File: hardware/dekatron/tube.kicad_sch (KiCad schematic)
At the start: 30 parts, among them J201 TUBE_ANODE, J202 TUBE, Q201 MMBTA42, Q202 MMBTA42, Q203 MMBTA92

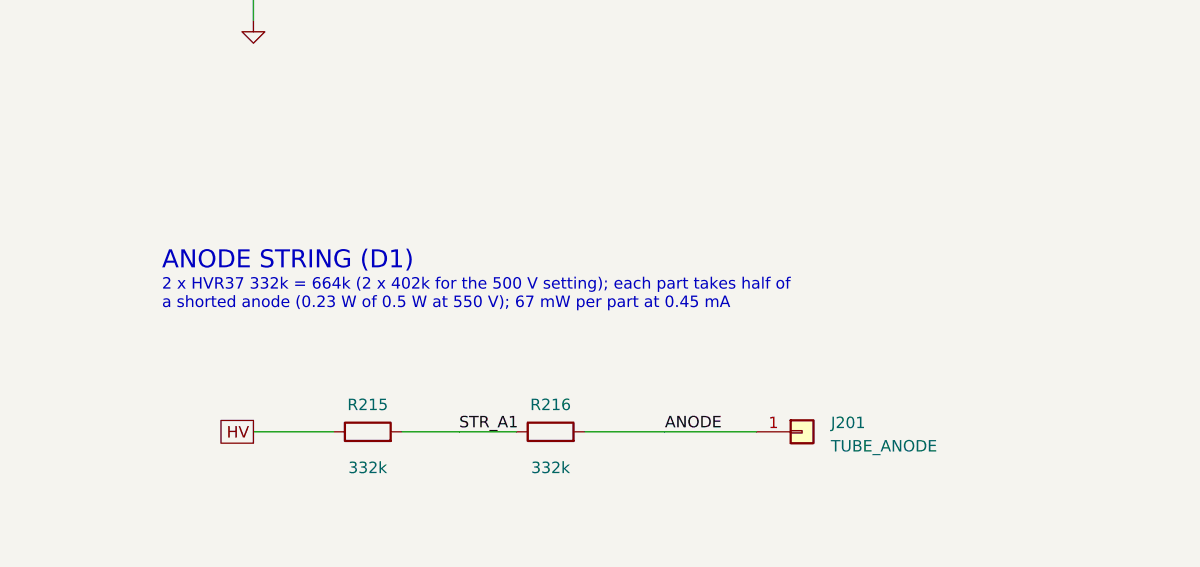
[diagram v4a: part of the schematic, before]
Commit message: Replace Vishay HVR25/HVR37 with Yageo HHV-25/HHV-50 (Mouser stock)
Same ratings (1600 V / 3500 V DC, 1 %, 200 ppm/K, 100k-68M E24/E96) and bodies
no larger (6.3 x 2.4 mm, 9.0 x 3.3 mm), so the 0207/0411 footprints stay.
Generator emits Yageo ordering codes (HHV-25FT-52-4M75 etc.); PCB fields
synced in place, ERC/DRC parity unchanged. hardware.md records the voltage
each leg actually needs at the 1.5x rule: >= 830 V for the two HV divider
tops, >= 415 V / 0.5 W for the anode pair, >= 303 V for the V_b-side parts.

Co-Authored-By: Claude Opus 5.5 <noreply@anthropic.com>
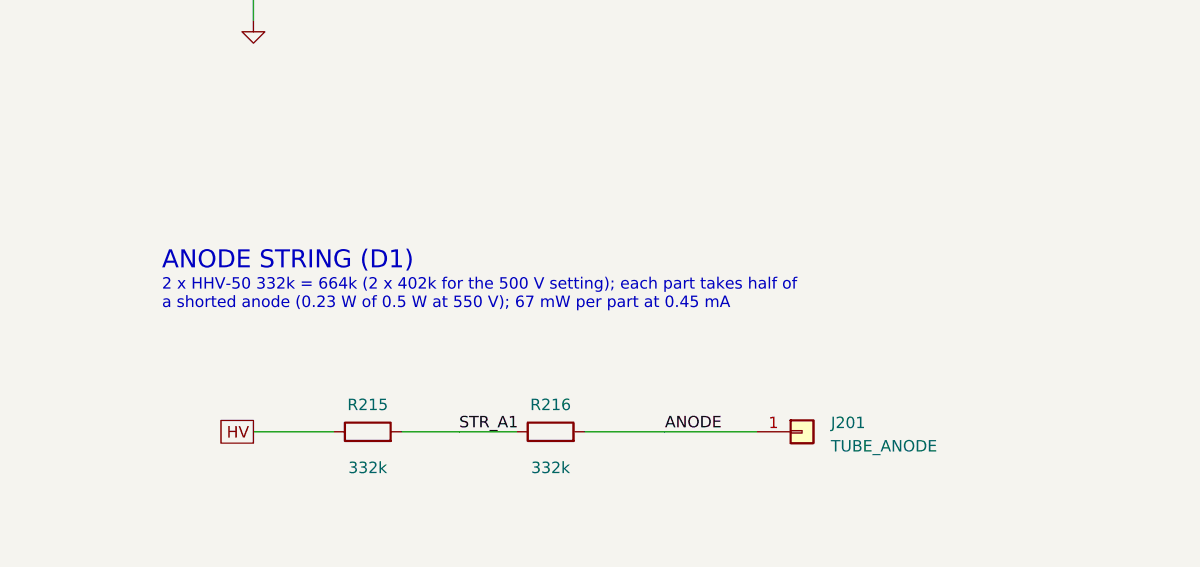
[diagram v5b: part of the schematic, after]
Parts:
- R202: MPN HVR2500002003FR500 -> HHV-25FT-52-200K; Manufacturer Vishay -> Yageo; Rating HVR25: 0.25 W, 1600 V DC, 1 %, 200 ppm/K -> HHV-25: 0.25 W, 1600 V DC, 1 %, 200 ppm/K
- R212: MPN HVR2500002203FR500 -> HHV-25FT-52-220K; Manufacturer Vishay -> Yageo; Rating HVR25: 0.25 W, 1600 V DC, 1 %, 200 ppm/K -> HHV-25: 0.25 W, 1600 V DC, 1 %, 200 ppm/K
- R215, R216: MPN HVR3700003323FR500 -> HHV-50FT-52-332K; Manufacturer Vishay -> Yageo; Rating HVR37: 0.5 W, 3500 V DC, 1 %, 200 ppm/K -> HHV-50: 0.5 W, 3500 V DC, 1 %, 200 ppm/K
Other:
- note added: "2 x HHV-50 332k = 664k (2 x 402k for the 500 V setting); each part takes half of a shorted anode (0.23 W of 0.5 W at 550 V); 67 mW per part at 0.45 mA"
- note removed: "2 x HVR37 332k = 664k (2 x 402k for the 500 V setting); each part takes half of a shorted anode (0.23 W of 0.5 W at 550 V); 67 mW per part at 0.45 mA"
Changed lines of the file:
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@@
 	  (property "Description" "Resistor" (at 25.4 102.87 0) (hide yes) (show_name no) (do_not_autoplace no) (effects (font (size 1.27 1.27)) (justify left)))
 	  (property "Function" "RTN_SENSE divider, upper (175 V if RTN fails to V_b)" (at 25.4 102.87 0) (hide yes) (show_name no) (do_not_autoplace no) (effects (font (size 1.27 1.27)) (justify left)))
-	  (property "MPN" "HVR2500002003FR500" (at 25.4 102.87 0) (hide yes) (show_name no) (do_not_autoplace no) (effects (font (size 1.27 1.27)) (justify left)))
-	  (property "Manufacturer" "Vishay" (at 25.4 102.87 0) (hide yes) (show_name no) (do_not_autoplace no) (effects (font (size 1.27 1.27)) (justify left)))
-	  (property "Rating" "HVR25: 0.25 W, 1600 V DC, 1 %, 200 ppm/K" (at 25.4 102.87 0) (hide yes) (show_name no) (do_not_autoplace no) (effects (font (size 1.27 1.27)) (justify left)))
+	  (property "MPN" "HHV-25FT-52-200K" (at 25.4 102.87 0) (hide yes) (show_name no) (do_not_autoplace no) (effects (font (size 1.27 1.27)) (justify left)))
+	  (property "Manufacturer" "Yageo" (at 25.4 102.87 0) (hide yes) (show_name no) (do_not_autoplace no) (effects (font (size 1.27 1.27)) (justify left)))
+	  (property "Rating" "HHV-25: 0.25 W, 1600 V DC, 1 %, 200 ppm/K" (at 25.4 102.87 0) (hide yes) (show_name no) (do_not_autoplace no) (effects (font (size 1.27 1.27)) (justify left)))
 	  (pin "1")
 	  (pin "2")
@@
 	  (property "Description" "Resistor" (at 86.36 186.69 0) (hide yes) (show_name no) (do_not_autoplace no) (effects (font (size 1.27 1.27)) (justify left)))
 	  (property "Function" "Index divider, upper (167 V fault)" (at 86.36 186.69 0) (hide yes) (show_name no) (do_not_autoplace no) (effects (font (size 1.27 1.27)) (justify left)))
-	  (property "MPN" "HVR2500002203FR500" (at 86.36 186.69 0) (hide yes) (show_name no) (do_not_autoplace no) (effects (font (size 1.27 1.27)) (justify left)))
-	  (property "Manufacturer" "Vishay" (at 86.36 186.69 0) (hide yes) (show_name no) (do_not_autoplace no) (effects (font (size 1.27 1.27)) (justify left)))
-	  (property "Rating" "HVR25: 0.25 W, 1600 V DC, 1 %, 200 ppm/K" (at 86.36 186.69 0) (hide yes) (show_name no) (do_not_autoplace no) (effects (font (size 1.27 1.27)) (justify left)))
+	  (property "MPN" "HHV-25FT-52-220K" (at 86.36 186.69 0) (hide yes) (show_name no) (do_not_autoplace no) (effects (font (size 1.27 1.27)) (justify left)))
+	  (property "Manufacturer" "Yageo" (at 86.36 186.69 0) (hide yes) (show_name no) (do_not_autoplace no) (effects (font (size 1.27 1.27)) (justify left)))
+	  (property "Rating" "HHV-25: 0.25 W, 1600 V DC, 1 %, 200 ppm/K" (at 86.36 186.69 0) (hide yes) (show_name no) (do_not_autoplace no) (effects (font (size 1.27 1.27)) (justify left)))
 	  (pin "1")
 	  (pin "2")
@@
 	(global_label "NDX" (shape passive) (at 114.3 200.66 0) (fields_autoplaced yes) (effects (font (size 1.27 1.27)) (justify left)) (property "Intersheetrefs" "${INTERSHEET_REFS}" (at 114.3 200.66 0) (effects (font (size 1.27 1.27)) (hide yes))))
 	(text "ANODE STRING (D1)" (exclude_from_sim no) (at 152.4 142.24 0) (effects (font (size 2.0 2.0)) (justify left bottom)))
-	(text "2 x HVR37 332k = 664k (2 x 402k for the 500 V setting); each part takes half of\na shorted anode (0.23 W of 0.5 W at 550 V); 67 mW per part at 0.45 mA" (exclude_from_sim no) (at 152.4 146.56 0) (effects (font (size 1.27 1.27)) (justify left bottom)))
+	(text "2 x HHV-50 332k = 664k (2 x 402k for the 500 V setting); each part takes half of\na shorted anode (0.23 W of 0.5 W at 550 V); 67 mW per part at 0.45 mA" (exclude_from_sim no) (at 152.4 146.56 0) (effects (font (size 1.27 1.27)) (justify left bottom)))
 	(text "TUBE HARNESS (D14)" (exclude_from_sim no) (at 205.74 76.2 0) (effects (font (size 2.0 2.0)) (justify left bottom)))
 	(text "Wires soldered to board and socket; cathodes tied at the socket" (exclude_from_sim no) (at 205.74 80.52 0) (effects (font (size 1.27 1.27)) (justify left bottom)))
@@
 	  (property "Description" "Resistor" (at 175.26 160.02 90) (hide yes) (show_name no) (do_not_autoplace no) (effects (font (size 1.27 1.27)) (justify left)))
 	  (property "Function" "Anode resistor 1/2" (at 175.26 160.02 90) (hide yes) (show_name no) (do_not_autoplace no) (effects (font (size 1.27 1.27)) (justify left)))
-	  (property "MPN" "HVR3700003323FR500" (at 175.26 160.02 90) (hide yes) (show_name no) (do_not_autoplace no) (effects (font (size 1.27 1.27)) (justify left)))
-	  (property "Manufacturer" "Vishay" (at 175.26 160.02 90) (hide yes) (show_name no) (do_not_autoplace no) (effects (font (size 1.27 1.27)) (justify left)))
-	  (property "Rating" "HVR37: 0.5 W, 3500 V DC, 1 %, 200 ppm/K" (at 175.26 160.02 90) (hide yes) (show_name no) (do_not_autoplace no) (effects (font (size 1.27 1.27)) (justify left)))
+	  (property "MPN" "HHV-50FT-52-332K" (at 175.26 160.02 90) (hide yes) (show_name no) (do_not_autoplace no) (effects (font (size 1.27 1.27)) (justify left)))
+	  (property "Manufacturer" "Yageo" (at 175.26 160.02 90) (hide yes) (show_name no) (do_not_autoplace no) (effects (font (size 1.27 1.27)) (justify left)))
+	  (property "Rating" "HHV-50: 0.5 W, 3500 V DC, 1 %, 200 ppm/K" (at 175.26 160.02 90) (hide yes) (show_name no) (do_not_autoplace no) (effects (font (size 1.27 1.27)) (justify left)))
 	  (pin "1")
 	  (pin "2")
@@
 	  (property "Description" "Resistor" (at 195.58 160.02 90) (hide yes) (show_name no) (do_not_autoplace no) (effects (font (size 1.27 1.27)) (justify left)))
 	  (property "Function" "Anode resistor 2/2" (at 195.58 160.02 90) (hide yes) (show_name no) (do_not_autoplace no) (effects (font (size 1.27 1.27)) (justify left)))
-	  (property "MPN" "HVR3700003323FR500" (at 195.58 160.02 90) (hide yes) (show_name no) (do_not_autoplace no) (effects (font (size 1.27 1.27)) (justify left)))
-	  (property "Manufacturer" "Vishay" (at 195.58 160.02 90) (hide yes) (show_name no) (do_not_autoplace no) (effects (font (size 1.27 1.27)) (justify left)))
-	  (property "Rating" "HVR37: 0.5 W, 3500 V DC, 1 %, 200 ppm/K" (at 195.58 160.02 90) (hide yes) (show_name no) (do_not_autoplace no) (effects (font (size 1.27 1.27)) (justify left)))
-	  (pin "1")
-	  (pin "2")
+	  (property "MPN" "HHV-50FT-52-332K" (at 195.58 160.02 90) (hide yes) (show_name no) (do_not_autoplace no) (effects (font (size 1.27 1.27)) (justify left)))
+	  (property "Manufacturer" "Yageo" (at 195.58 160.02 90) (hide yes) (show_name no) (do_not_autoplace no) (effects (font (size 1.27 1.27)) (justify left)))
+	  (property "Rating" "HHV-50: 0.5 W, 3500 V DC, 1 %, 200 ppm/K" (at 195.58 160.02 90) (hide yes) (show_name no) (do_not_autoplace no) (effects (font (size 1.27 1.27)) (justify left)))
+	  (pin "1")
+	  (pin "2")

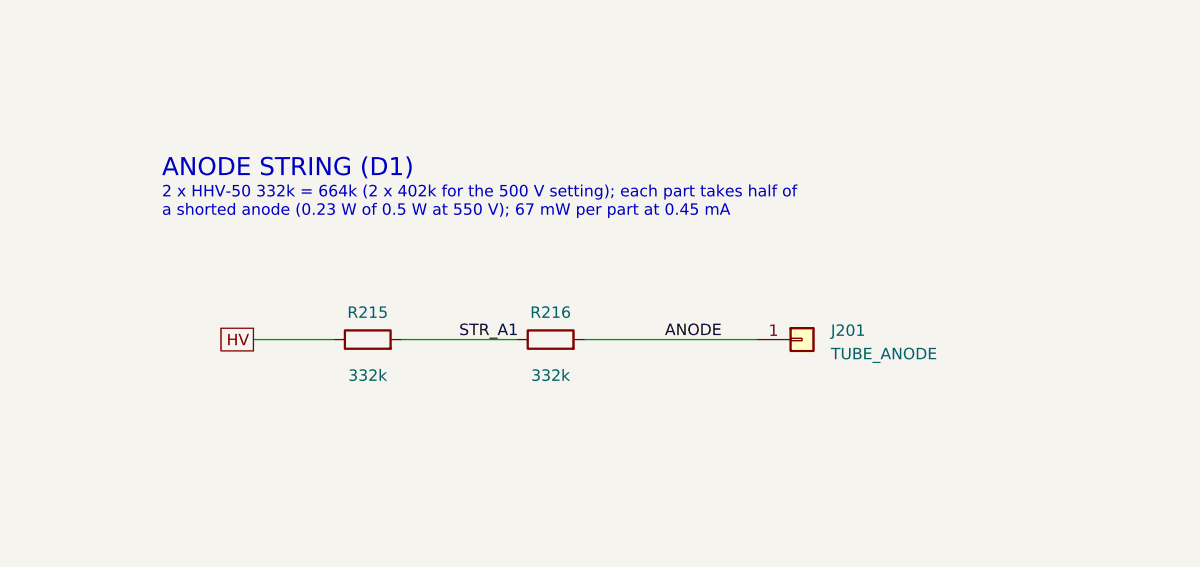
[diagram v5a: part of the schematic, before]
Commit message: Use E12 values for the Yageo HHV high-voltage resistors
HHV stock at Mouser follows E12 (2.2M/2.7M stocked, 2.0M/2.4M/332k not).
HHV parts now: 4.7M x2 (feedback, monitor/OVP tops), 2.2M x2 (V_b bleeder,
V_b OVP top), 220k (index), 330k x2 (anode, = D1's 660k design value);
R202 stays 200k (stocked, already ordered). Trims moved to 1206 bottoms:
feedback 10.4k -> 452.9 V (9.53k: 494.2 V); OVP 10.7k -> 548.4 V trip,
HV_SENSE = HV/191.3; V_b OVP 13.7k -> 200.7 V. 500 V anode option 330k +
470k = 800k; off-board dummy load 1M.

Re-simulated: 500 V setting regulates at 494.1 V out of current limit
(tube 368 uA, peaks HV 498 V, V_b 170 V); dark-tube feedback-open fault trips
at 550.3 V, bursts 547.1-549.7 V; open tripler diode holds V_b <= 198.4 V;
discharge < 50 V in 1.94 / 3.93 / 3.47 s. PCB fields synced, ERC/DRC
parity unchanged; footprints and fab files unchanged.

Co-Authored-By: Claude Opus 5.5 <noreply@anthropic.com>
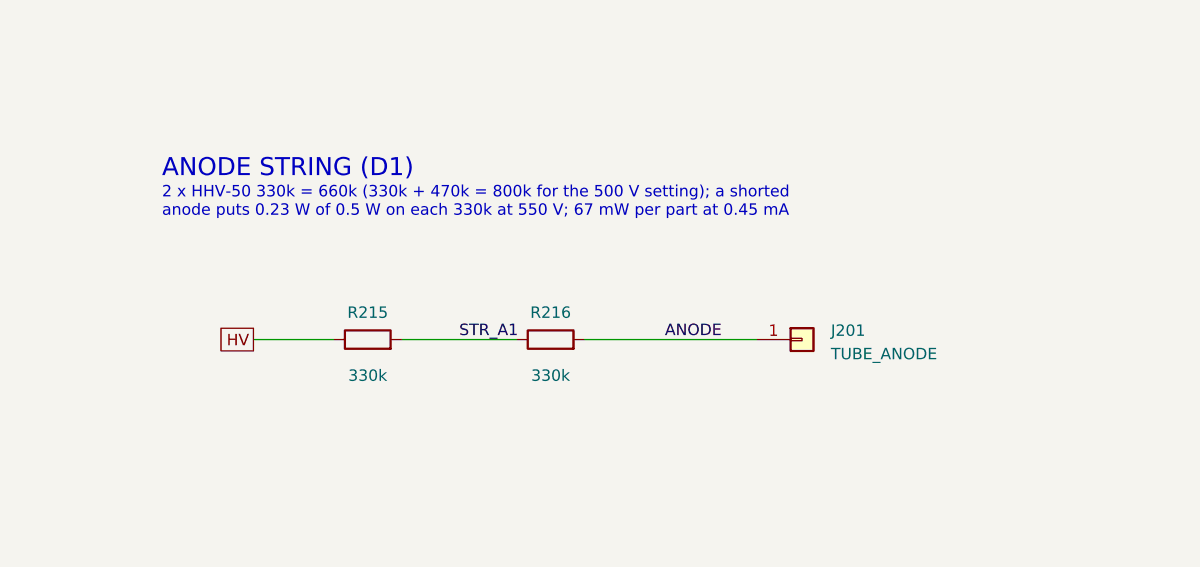
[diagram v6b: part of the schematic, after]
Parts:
- R215, R216: value 332k -> 330k; MPN HHV-50FT-52-332K -> HHV-50FT-52-330K
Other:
- note added: "2 x HHV-50 330k = 660k (330k + 470k = 800k for the 500 V setting); a shorted anode puts 0.23 W of 0.5 W on each 330k at 550 V; 67 mW per part at 0.45 mA"
- note removed: "2 x HHV-50 332k = 664k (2 x 402k for the 500 V setting); each part takes half of a shorted anode (0.23 W of 0.5 W at 550 V); 67 mW per part at 0.45 mA"
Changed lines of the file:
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@@
 	(global_label "NDX" (shape passive) (at 114.3 200.66 0) (fields_autoplaced yes) (effects (font (size 1.27 1.27)) (justify left)) (property "Intersheetrefs" "${INTERSHEET_REFS}" (at 114.3 200.66 0) (effects (font (size 1.27 1.27)) (hide yes))))
 	(text "ANODE STRING (D1)" (exclude_from_sim no) (at 152.4 142.24 0) (effects (font (size 2.0 2.0)) (justify left bottom)))
-	(text "2 x HHV-50 332k = 664k (2 x 402k for the 500 V setting); each part takes half of\na shorted anode (0.23 W of 0.5 W at 550 V); 67 mW per part at 0.45 mA" (exclude_from_sim no) (at 152.4 146.56 0) (effects (font (size 1.27 1.27)) (justify left bottom)))
+	(text "2 x HHV-50 330k = 660k (330k + 470k = 800k for the 500 V setting); a shorted\nanode puts 0.23 W of 0.5 W on each 330k at 550 V; 67 mW per part at 0.45 mA" (exclude_from_sim no) (at 152.4 146.56 0) (effects (font (size 1.27 1.27)) (justify left bottom)))
 	(text "TUBE HARNESS (D14)" (exclude_from_sim no) (at 205.74 76.2 0) (effects (font (size 2.0 2.0)) (justify left bottom)))
 	(text "Wires soldered to board and socket; cathodes tied at the socket" (exclude_from_sim no) (at 205.74 80.52 0) (effects (font (size 1.27 1.27)) (justify left bottom)))
 	(symbol (lib_id "Device:R") (at 175.26 160.02 90) (unit 1) (body_style 1) (exclude_from_sim no) (in_bom yes) (on_board yes) (in_pos_files yes) (dnp no)
 	  (property "Reference" "R215" (at 175.26 157.02 90) (show_name no) (do_not_autoplace no) (effects (font (size 1.27 1.27))))
-	  (property "Value" "332k" (at 175.26 164.02 90) (show_name no) (do_not_autoplace no) (effects (font (size 1.27 1.27))))
+	  (property "Value" "330k" (at 175.26 164.02 90) (show_name no) (do_not_autoplace no) (effects (font (size 1.27 1.27))))
 	  (property "Footprint" "Resistor_THT:R_Axial_DIN0411_L9.9mm_D3.6mm_P15.24mm_Horizontal" (at 175.26 160.02 90) (hide yes) (show_name no) (do_not_autoplace no) (effects (font (size 1.27 1.27)) (justify left)))
 	  (property "Datasheet" "" (at 175.26 160.02 90) (hide yes) (show_name no) (do_not_autoplace no) (effects (font (size 1.27 1.27)) (justify left)))
 	  (property "Description" "Resistor" (at 175.26 160.02 90) (hide yes) (show_name no) (do_not_autoplace no) (effects (font (size 1.27 1.27)) (justify left)))
 	  (property "Function" "Anode resistor 1/2" (at 175.26 160.02 90) (hide yes) (show_name no) (do_not_autoplace no) (effects (font (size 1.27 1.27)) (justify left)))
-	  (property "MPN" "HHV-50FT-52-332K" (at 175.26 160.02 90) (hide yes) (show_name no) (do_not_autoplace no) (effects (font (size 1.27 1.27)) (justify left)))
+	  (property "MPN" "HHV-50FT-52-330K" (at 175.26 160.02 90) (hide yes) (show_name no) (do_not_autoplace no) (effects (font (size 1.27 1.27)) (justify left)))
 	  (property "Manufacturer" "Yageo" (at 175.26 160.02 90) (hide yes) (show_name no) (do_not_autoplace no) (effects (font (size 1.27 1.27)) (justify left)))
 	  (property "Rating" "HHV-50: 0.5 W, 3500 V DC, 1 %, 200 ppm/K" (at 175.26 160.02 90) (hide yes) (show_name no) (do_not_autoplace no) (effects (font (size 1.27 1.27)) (justify left)))
@@
 	(symbol (lib_id "Device:R") (at 195.58 160.02 90) (unit 1) (body_style 1) (exclude_from_sim no) (in_bom yes) (on_board yes) (in_pos_files yes) (dnp no)
 	  (property "Reference" "R216" (at 195.58 157.02 90) (show_name no) (do_not_autoplace no) (effects (font (size 1.27 1.27))))
-	  (property "Value" "332k" (at 195.58 164.02 90) (show_name no) (do_not_autoplace no) (effects (font (size 1.27 1.27))))
+	  (property "Value" "330k" (at 195.58 164.02 90) (show_name no) (do_not_autoplace no) (effects (font (size 1.27 1.27))))
 	  (property "Footprint" "Resistor_THT:R_Axial_DIN0411_L9.9mm_D3.6mm_P15.24mm_Horizontal" (at 195.58 160.02 90) (hide yes) (show_name no) (do_not_autoplace no) (effects (font (size 1.27 1.27)) (justify left)))
 	  (property "Datasheet" "" (at 195.58 160.02 90) (hide yes) (show_name no) (do_not_autoplace no) (effects (font (size 1.27 1.27)) (justify left)))
 	  (property "Description" "Resistor" (at 195.58 160.02 90) (hide yes) (show_name no) (do_not_autoplace no) (effects (font (size 1.27 1.27)) (justify left)))
 	  (property "Function" "Anode resistor 2/2" (at 195.58 160.02 90) (hide yes) (show_name no) (do_not_autoplace no) (effects (font (size 1.27 1.27)) (justify left)))
-	  (property "MPN" "HHV-50FT-52-332K" (at 195.58 160.02 90) (hide yes) (show_name no) (do_not_autoplace no) (effects (font (size 1.27 1.27)) (justify left)))
+	  (property "MPN" "HHV-50FT-52-330K" (at 195.58 160.02 90) (hide yes) (show_name no) (do_not_autoplace no) (effects (font (size 1.27 1.27)) (justify left)))
 	  (property "Manufacturer" "Yageo" (at 195.58 160.02 90) (hide yes) (show_name no) (do_not_autoplace no) (effects (font (size 1.27 1.27)) (justify left)))
 	  (property "Rating" "HHV-50: 0.5 W, 3500 V DC, 1 %, 200 ppm/K" (at 195.58 160.02 90) (hide yes) (show_name no) (do_not_autoplace no) (effects (font (size 1.27 1.27)) (justify left)))

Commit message: Freeze the dekatron BOM to the Mouser order; substitutions; re-route
- ORDERED_PARTS in gen_schematics.py: exact manufacturer part numbers from
  Cart_Oct08_0432PM.xls (committed as the record), overriding design-time MPNs
- Backorder substitutions: TPS54302 (pin-compatible 5 V buck), IPD70R1K4P7S
  (700 V CoolMOS P7, replaces the EOL IPD50R1K4CE), MMSZ5262BT1G, BAT54S RFG
- C301 is the user's F91 tantalum: polarised symbol and EIA 3216-18 footprint
- E24 dividers: HV feedback 2 x 3.0k 0805 (451.0 V; 2 x 2.7k for 500 V),
  OVP lower 6.2k (543.7 V); simulations re-run, docs updated
- Router: exact own-pad clearance, D301 GND escape via kept out of the
  RP2040 no-via area (D301 anchored rotated), 0.3 mm GND repair links
- Full re-route, DRC clean (expected U106 mismatch, one starved thermal);
  fab outputs regenerated

Co-Authored-By: Claude Opus 5.5 <noreply@anthropic.com>
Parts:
- C201: MPN (none) -> AC1206KKX7R0BB104; Manufacturer (none) -> Yageo
- C202: MPN (none) -> C1206C105M1RACAUTO; Manufacturer (none) -> KEMET
- C204: MPN (none) -> 1206N102K501CT; Manufacturer (none) -> Walsin
- D201: MPN MMSZ5259B -> MMSZ5259BH RHG; Manufacturer onsemi -> Taiwan Semiconductor
- D202: MPN MMSZ5262B -> MMSZ5262BT1G
- Q201, Q202, Q203: Manufacturer Nexperia -> Diotec Semiconductor
- R202: MPN HHV-25FT-52-200K -> HHV-25FR-52-200K
- R212: MPN HHV-25FT-52-220K -> HHV-25FR-52-220K
- R214: MPN (none) -> CR1206-FX-1302ELF; Manufacturer (none) -> Bourns
- R215, R216: MPN HHV-50FT-52-330K -> HHV-50FR-52-330K
